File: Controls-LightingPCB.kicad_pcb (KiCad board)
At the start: 2 copper layers, 80.3 x 98.8 mm, 92 parts, among them J1 MinionConn, J10 INTERNAL_RIGHTBLINK, J11 INTERNAL_LEFTBLINK, J12 EXTERNAL_RIGHTBLINK, J13 EXTERNAL_HDLT, J14 EXTERNAL_BRAKELIGHT, J2 12VPWRCONN, J3 CRUZ_ST_INDICATOR_33v, J4 CRUZ_EN_INDICATOR_33v, J5 REGEN_INDICATOR_33v, J6 NEU_INDICATOR_33v, J7 FOR_INDICATOR_33v, J8 REV_INDICATOR_33v, J9 EXTERNAL_LEFTBLINK, Q1 2N7000, Q2 2N7000, Q3 2N7000, Q4 2N7000, Q5 2N7000, SW1 CRUISE_SET, SW2 CRUISE_ENABLE, SW3 F/R_SW, SW4 REGEN_SW, SW5 TURN_SIGNAL_SW, U1 NCP1117-3.3_SOT223

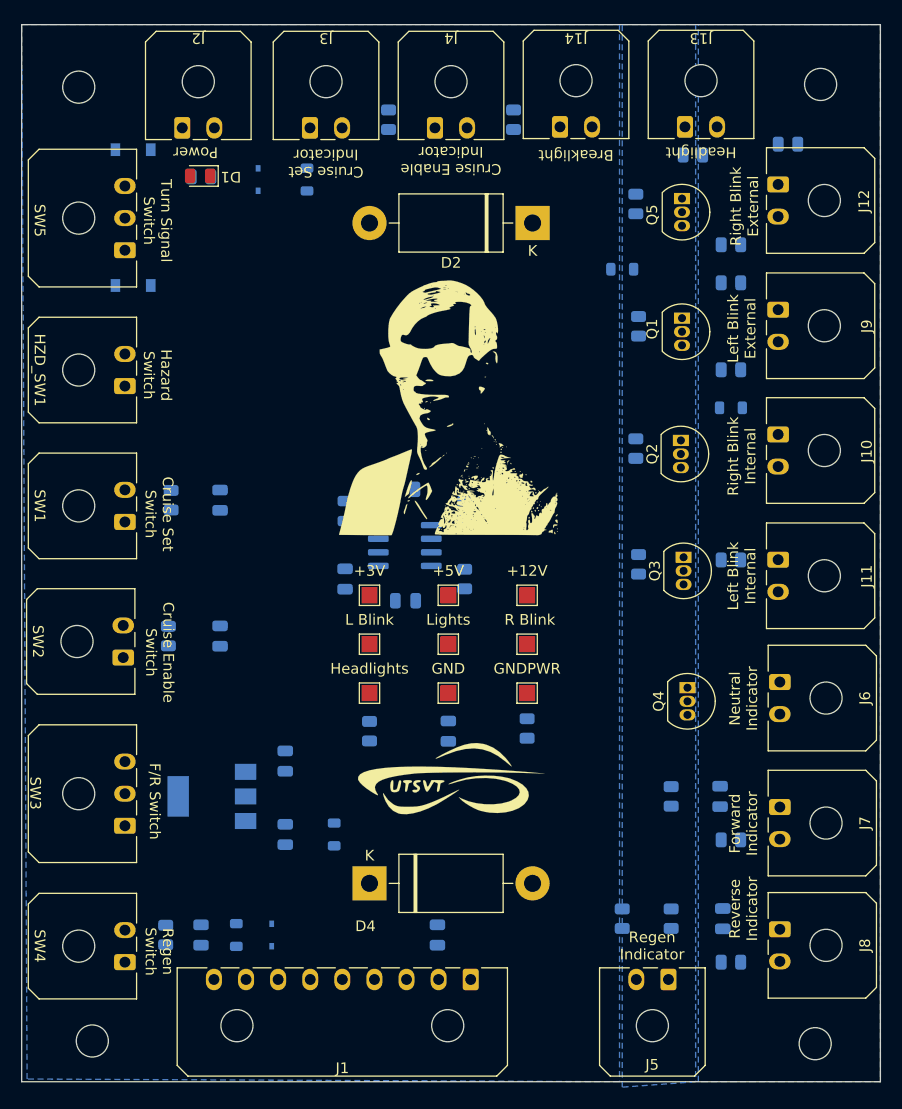
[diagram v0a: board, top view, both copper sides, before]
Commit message: Pico-Claps connectors + traces
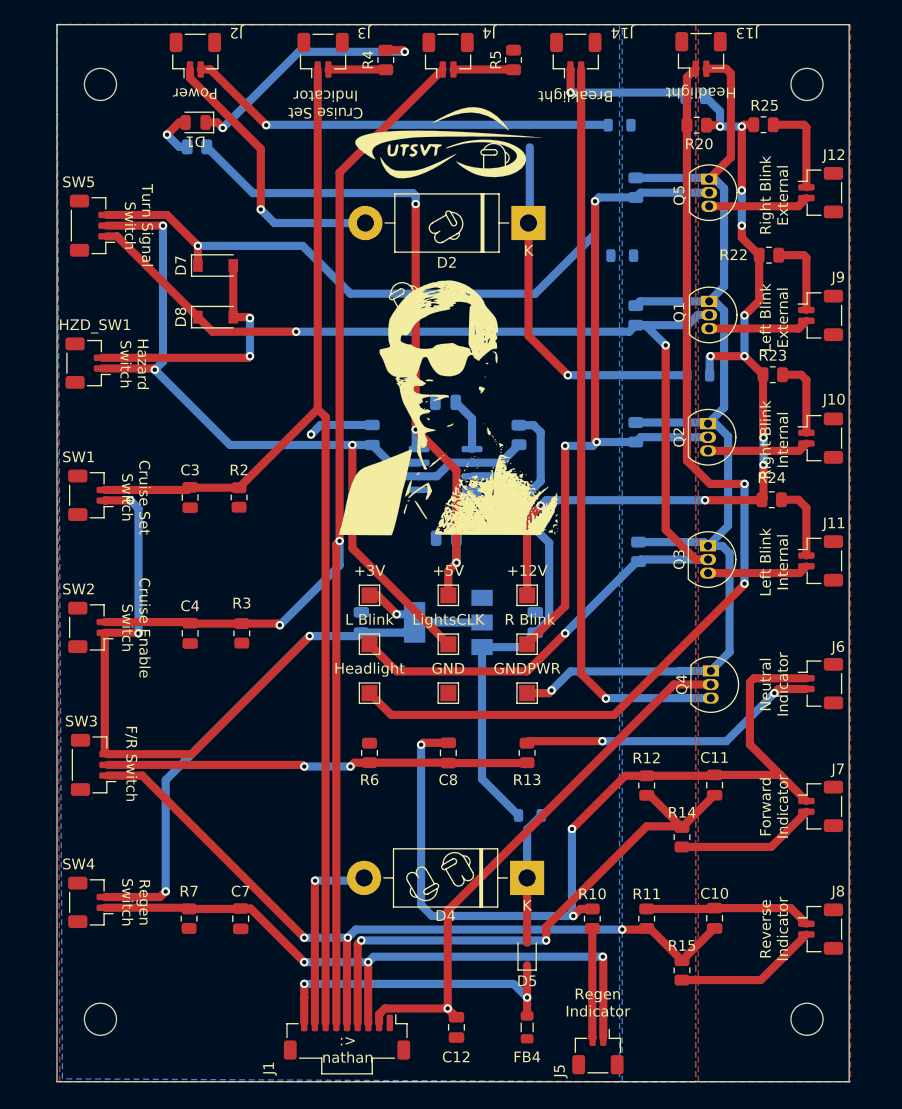
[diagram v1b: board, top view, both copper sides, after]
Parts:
- C10, C11, C12, C3, C4, C7, C8, D5, D7, D8, FB4, R10, R11, R12, R13, R14, R15, R2, R20, R22, R23, R24, R25, R3, R4, R5, R6, R7: moved to F.Cu
- HZD_SW1, J10, J11, J12, J13, J14, J2, J3, J4, J5, J6, J7, J8, J9, SW1, SW2, SW4: footprint Connector_Molex:Molex_Micro-Fit_3.0_43650-0200_1x02_P3.00mm_Horizontal -> Connector_Molex:Molex_Pico-Clasp_501331-0207_1x02-1MP_P1.00mm_Vertical
- J1: footprint Connector_Molex:Molex_Micro-Fit_3.0_43650-0900_1x09_P3.00mm_Horizontal -> Connector_Molex:Molex_Pico-Clasp_501331-0907_1x09-1MP_P1.00mm_Vertical
- SW3, SW5: footprint Connector_Molex:Molex_Micro-Fit_3.0_43650-0300_1x03_P3.00mm_Horizontal -> Connector_Molex:Molex_Pico-Clasp_501331-0307_1x03-1MP_P1.00mm_Vertical
- moved LOGO2 59.4 mm to (144.0, 55.1)
- moved C1 30.6 mm to (152.4, 99.8), turned to 90 degrees
- moved FB2 29.6 mm to (160.3, 53.3), turned to 0 degrees
- moved FB4 28.5 mm to (151.6, 137.7), turned to -90 degrees
- moved U1 27.4 mm to (144.3, 99.8)
- moved D3 25.7 mm to (151.9, 54.4)
- moved D5 23.9 mm to (151.6, 130.8)
- moved FB3 18.4 mm to (151.9, 117.9), turned to 180 degrees
- moved C2 14.8 mm to (136.1, 99.8)
- moved D4 14.7 mm to (151.6, 123.7), turned to 180 degrees
- moved R21 14.2 mm to (167.4, 50.7)
- moved D7 13.3 mm to (122.5, 66.5)
- moved J1 12.8 mm to (134.8, 138.6)
- moved J5 9.44 mm to (158.3, 140.0)
- moved C5 8.98 mm to (144.0, 79.2)
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- renumbered Headlights to Headlight, Lights to LightsCLK
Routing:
- net GND: track 0.00 -> 128.0 mm, vias 0 -> 6
- net /LEFT_BLINK: track 0.07 -> 123.6 mm, vias 0 -> 3
- net /RIGHT_BLINK: track 0.00 -> 123.2 mm, vias 0 -> 4
- net /CRUZ_EN: track 0.00 -> 119.9 mm, vias 0 -> 2
- net /CRUZ_ST: track 0.00 -> 112.5 mm
- net GNDPWR: track 0.26 -> 111.8 mm, vias 0 -> 1
- net +5V: track 0.00 -> 110.9 mm, vias 0 -> 3
- net +3V3: track 0.00 -> 110.5 mm, vias 0 -> 5
- net /HEADLIGHT_SW: track 0.03 -> 93.6 mm, vias 0 -> 2
- net +12V: track 0.00 -> 80.0 mm, vias 0 -> 11
- net /LIGHTSCLK: track 0.00 -> 74.7 mm, vias 0 -> 3
- net /REV_SW: track 0.00 -> 73.9 mm, vias 0 -> 3
- net Net-(J14-Pad2): track 0.00 -> 69.6 mm, vias 0 -> 1
- net /REGEN_SW: track 0.00 -> 62.2 mm, vias 0 -> 3
- net /FOR_SW: track 0.00 -> 51.9 mm, vias 0 -> 2
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- added copper zone on F.Cu, net +12V
- added copper zone on F.Cu, net GND
- removed copper zone on B.Cu, net +12V
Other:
- board size 80.3 x 98.8 mm -> 74 x 98.8 mm
- board text added: ":> nathan"
- board text removed: "Cruise Enable Indicator"

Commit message: Changes to traces/silkscreens
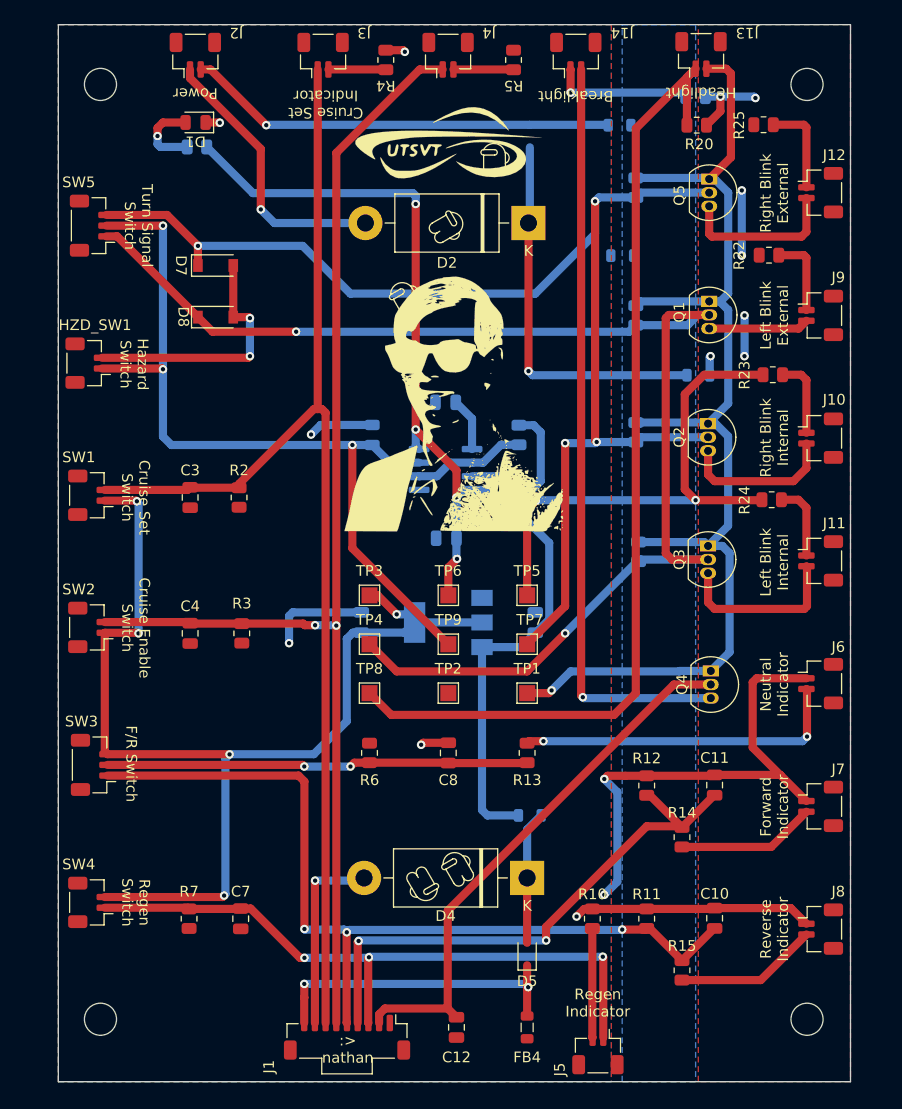
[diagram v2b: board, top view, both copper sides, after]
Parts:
- TP4: renamed from L Blink
- TP7: renamed from R Blink
- moved LOGO1 0.62 mm to (143.9, 79.1)
- renumbered GNDPWR to TP1, GND to TP2, +3V to TP3, +12V to TP5, +5V to TP6, Headlight to TP8, LightsCLK to TP9
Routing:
- net GND: track 128.0 -> 90.5 mm, vias 6 -> 8
- net +12V: track 80.0 -> 68.5 mm, vias 11 -> 9
- net /REV_SW: track 73.9 -> 82.0 mm
- net Net-(J11-Pad2): track 9.46 -> 16.1 mm
- net +3V3: track 110.5 -> 104.6 mm
- net Net-(J12-Pad2): track 9.41 -> 15.1 mm
- net Net-(J10-Pad2): track 9.48 -> 14.5 mm
- net /LEFT_BLINK: track 123.6 -> 128.1 mm, vias 3 -> 2
- net +5V: track 110.9 -> 107.0 mm, vias 3 -> 4
- net /CRUZ_EN: track 119.9 -> 116.3 mm
- net /LIGHTSCLK: track 74.7 -> 78.0 mm
- net Net-(J6-Pad2): track 28.2 -> 30.9 mm
- net Net-(D1-Pad2): track 4.56 -> 6.97 mm
- net Net-(D2-Pad1): track 34.0 -> 35.9 mm
- net /HEADLIGHT_SW: track 93.6 -> 92.4 mm, vias 2 -> 0
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
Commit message: edge cuts
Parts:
- moved H3 1.80 mm to (112.0, 138.7)
- moved H4 1.78 mm to (177.8, 138.7)
- moved H1 1.55 mm to (112.0, 48.0)
- moved H2 1.52 mm to (177.8, 48.0)
- moved SW3 0.35 mm to (110.7, 113.1)
- moved SW5 0.25 mm to (110.7, 62.7)
- moved HZD_SW1 0.16 mm to (110.7, 75.6)
- moved SW1 0.09 mm to (110.7, 87.9)
- moved SW2 0.09 mm to (110.7, 100.3)
- moved SW4 0.09 mm to (110.7, 126.0)
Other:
- board size 74 x 98.8 mm -> 73.9 x 98.8 mm
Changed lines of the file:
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@@
   (net 44 "Net-(D7-Pad2)")
   (footprint "Connector_Molex:Molex_Pico-Clasp_501331-0307_1x03-1MP_P1.00mm_Vertical" (layer "F.Cu")
-    (at 111.092 113.132855 90)
+    (at 110.744 113.132855 90)
     (descr "Molex Pico-Clasp series connector, 501331-0307 (http://www.molex.com/pdm_docs/sd/5013310207_sd.pdf), generated with kicad-footprint-generator")
     (tags "connector Molex Pico-Clasp side entry")
@@
   )
   (footprint "MountingHole:MountingHole_3mm" (layer "F.Cu")
-    (at 111.76 49.53)
+    (at 112.014 48.006)
     (descr "Mounting Hole 3mm, no annular")
     (tags "mounting hole 3mm no annular")
@@
       (net 41 "/HEADLIGHT_SW") (pinfunction "1") (pintype "passive"))
   )
-  (footprint "MountingHole:MountingHole_3mm" locked (layer "F.Cu")
-    (at 177.8 49.53)
+  (footprint "MountingHole:MountingHole_3mm" (layer "F.Cu")
+    (at 177.8 48.006)
     (descr "Mounting Hole 3mm, no annular")
     (tags "mounting hole 3mm no annular")
@@
   )
   (footprint "Connector_Molex:Molex_Pico-Clasp_501331-0207_1x02-1MP_P1.00mm_Vertical" (layer "F.Cu")
-    (at 110.584 75.581142 90)
+    (at 110.744 75.581142 90)
     (descr "Molex Pico-Clasp series connector, 501331-0207 (http://www.molex.com/pdm_docs/sd/5013310207_sd.pdf), generated with kicad-footprint-generator")
     (tags "connector Molex Pico-Clasp side entry")
@@
   )
   (footprint "Connector_Molex:Molex_Pico-Clasp_501331-0307_1x03-1MP_P1.00mm_Vertical" (layer "F.Cu")
-    (at 110.998 62.730571 90)
+    (at 110.744 62.730571 90)
     (descr "Molex Pico-Clasp series connector, 501331-0307 (http://www.molex.com/pdm_docs/sd/5013310207_sd.pdf), generated with kicad-footprint-generator")
     (tags "connector Molex Pico-Clasp side entry")
@@
   )
   (footprint "MountingHole:MountingHole_3mm" (layer "F.Cu")
-    (at 111.76 136.906)
+    (at 112.014 138.684)
     (descr "Mounting Hole 3mm, no annular")
     (tags "mounting hole 3mm no annular")
@@
   )
   (footprint "Connector_Molex:Molex_Pico-Clasp_501331-0207_1x02-1MP_P1.00mm_Vertical" (layer "F.Cu")
-    (at 110.838 125.983426 90)
+    (at 110.744 125.983426 90)
     (descr "Molex Pico-Clasp series connector, 501331-0207 (http://www.molex.com/pdm_docs/sd/5013310207_sd.pdf), generated with kicad-footprint-generator")
     (tags "connector Molex Pico-Clasp side entry")
@@
   )
   (footprint "Connector_Molex:Molex_Pico-Clasp_501331-0207_1x02-1MP_P1.00mm_Vertical" (layer "F.Cu")
-    (at 110.838 100.282284 90)
+    (at 110.744 100.282284 90)
     (descr "Molex Pico-Clasp series connector, 501331-0207 (http://www.molex.com/pdm_docs/sd/5013310207_sd.pdf), generated with kicad-footprint-generator")
     (tags "connector Molex Pico-Clasp side entry")
@@
     )
   )
-  (footprint "MountingHole:MountingHole_3mm" locked (layer "F.Cu")
-    (at 177.8 136.906)
+  (footprint "MountingHole:MountingHole_3mm" (layer "F.Cu")
+    (at 177.8 138.684)
     (descr "Mounting Hole 3mm, no annular")
     (tags "mounting hole 3mm no annular")
@@
   )
   (footprint "Connector_Molex:Molex_Pico-Clasp_501331-0207_1x02-1MP_P1.00mm_Vertical" (layer "F.Cu")
-    (at 110.838 87.931713 90)
+    (at 110.744 87.931713 90)
     (descr "Molex Pico-Clasp series connector, 501331-0207 (http://www.molex.com/pdm_docs/sd/5013310207_sd.pdf), generated with kicad-footprint-generator")
     (tags "connector Molex Pico-Clasp side entry")
@@
   (gr_arc (start 144.036236 122.886177) (mid 143.689266 122.793207) (end 143.782236 122.446236) (layer "F.SilkS") (width 0.12))
   (gr_arc (start 143.782236 122.446236) (mid 144.564232 121.372056) (end 145.796 121.870177) (layer "F.SilkS") (width 0.12))
-  (gr_rect (start 181.864 43.942) (end 107.823 142.748) (layer "Edge.Cuts") (width 0.05) (fill none))
+  (gr_line (start 181.864 48.006) (end 181.864 138.684) (layer "Edge.Cuts") (width 0.05))
+  (gr_line (start 107.95 138.684) (end 107.95 48.006) (layer "Edge.Cuts") (width 0.05))
+  (gr_line (start 177.8 142.748) (end 112.014 142.748) (layer "Edge.Cuts") (width 0.05))
+  (gr_arc (start 177.8 43.942) (mid 180.673682 45.132318) (end 181.864 48.006) (layer "Edge.Cuts") (width 0.05))
+  (gr_line (start 112.014 43.942) (end 177.8 43.942) (layer "Edge.Cuts") (width 0.05))
+  (gr_arc (start 181.864 138.684) (mid 180.673682 141.557682) (end 177.8 142.748) (layer "Edge.Cuts") (width 0.05))
+  (gr_arc (start 107.95 48.006) (mid 109.140318 45.132318) (end 112.014 43.942) (layer "Edge.Cuts") (width 0.05))
+  (gr_arc (start 112.014 142.748) (mid 109.140318 141.557682) (end 107.95 138.684) (layer "Edge.Cuts") (width 0.05))
   (gr_text ":>\nnathan" (at 134.874 139.7) (layer "F.SilkS")
     (effects (font (size 1 1) (thickness 0.15)))
@@
     (effects (font (size 1 1) (thickness 0.25)))
   )
-  (gr_text "Turn Signal\nSwitch" (at 115.316 62.738 270) (layer "F.SilkS")
+  (gr_text "Turn Signal\nSwitch" (at 115.062 62.738 270) (layer "F.SilkS")
     (effects (font (size 1 1) (thickness 0.25)))
   )
@@
     (effects (font (size 1 1) (thickness 0.25)))
   )
-  (gr_text "Hazard\nSwitch" (at 114.902 75.692 270) (layer "F.SilkS")
+  (gr_text "Hazard\nSwitch" (at 115.062 75.692 270) (layer "F.SilkS")
     (effects (font (size 1 1) (thickness 0.25)))
   )

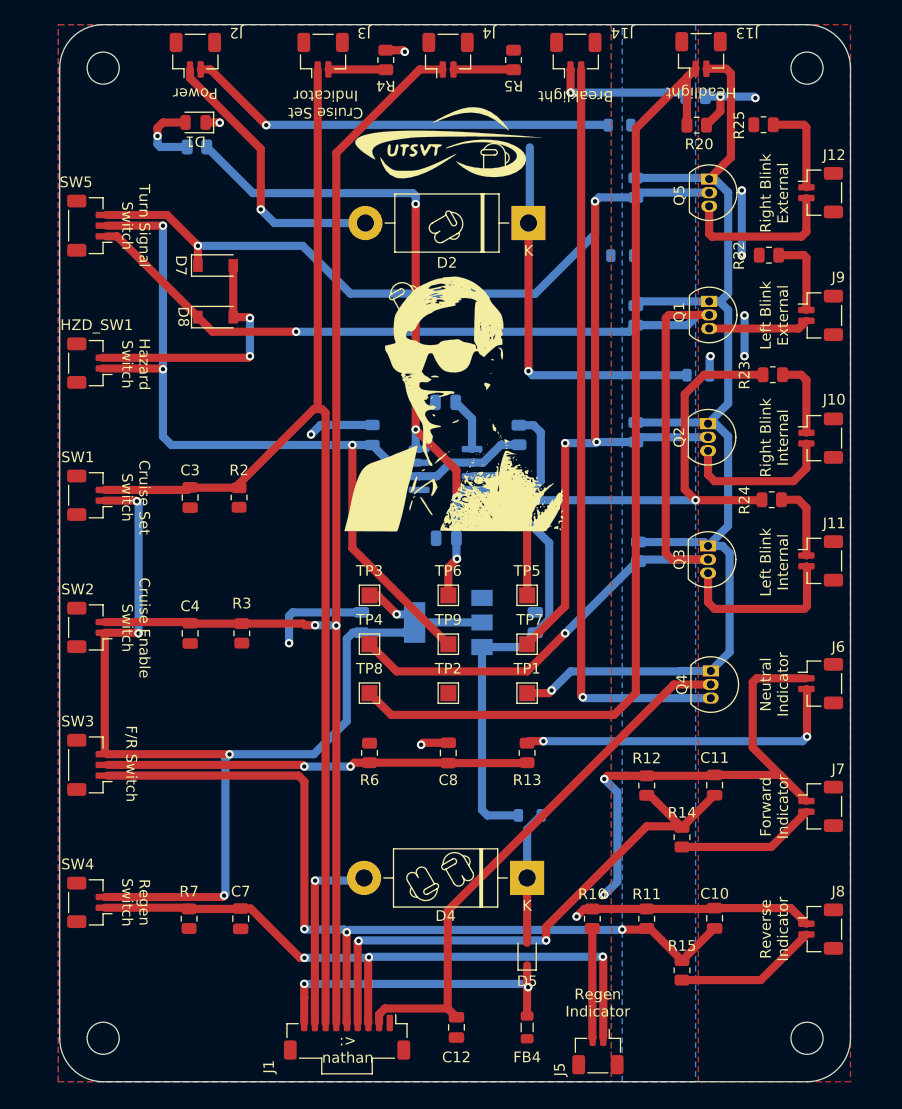
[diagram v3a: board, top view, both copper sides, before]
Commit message: moved components to front, fixed traces/planes
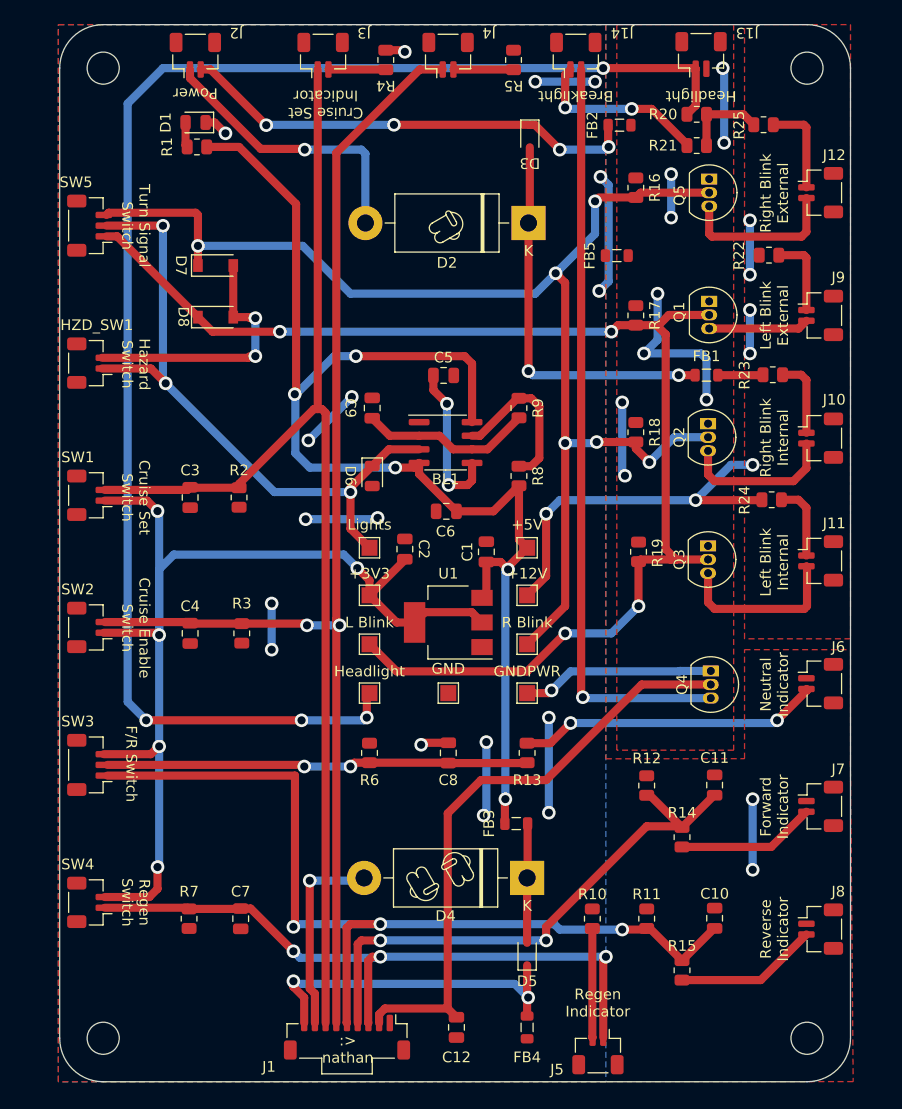
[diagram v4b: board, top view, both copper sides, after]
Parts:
- BL1, C1, C2, C5, C6, C9, D3, D6, FB1, FB2, FB3, FB5, R1, R16, R17, R18, R19, R21, R8, R9, U1: moved to F.Cu
- L Blink: renamed from TP4
- LOGO1, LOGO2: moved to B.Cu
- R Blink: renamed from TP7
- moved LOGO2 40.8 mm to (145.0, 95.9), turned to 180 degrees
- moved Lights 11.6 mm to (136.9, 92.8)
- moved C9 8.87 mm to (137.2, 79.8), turned to 90 degrees
- moved +5V 8.60 mm to (151.6, 92.8)
- moved C1 8.03 mm to (147.8, 93.2)
- moved C2 7.97 mm to (140.2, 93.0)
- moved R21 4.57 mm to (167.5, 55.2)
- moved D6 3.83 mm to (137.2, 86.1), turned to -90 degrees
- moved C5 2.52 mm to (143.8, 76.7), turned to 0 degrees
- moved R8 2.52 mm to (150.9, 86.1)
- moved R9 2.52 mm to (150.9, 79.8)
- moved BL1 2.52 mm to (144.0, 83.0)
- moved C6 2.52 mm to (144.1, 89.4)
- moved LOGO1 1.66 mm to (145.6, 79.1), turned to 180 degrees
- moved FB3 1.48 mm to (150.6, 118.6)
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- renumbered TP5 to +12V, TP3 to +3V3, TP6 to +5V, TP2 to GND, TP1 to GNDPWR, TP8 to Headlight, TP9 to Lights
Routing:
- net GNDPWR: track 112.3 -> 52.1 mm, vias 1 -> 10
- net /HEADLIGHT_SW: track 92.4 -> 140.6 mm, vias 0 -> 4
- net GND: track 90.5 -> 63.2 mm, vias 8 -> 19
- net /LIGHTSCLK: track 78.0 -> 62.4 mm
- net +5V: track 107.0 -> 121.4 mm, vias 4 -> 5
- net +12V: track 68.5 -> 56.8 mm, vias 9 -> 7
- net Net-(BL1-Pad5): track 5.00 -> 14.8 mm, vias 0 -> 2
- net /LEFT_BLINK: track 128.1 -> 122.7 mm, vias 2 -> 4
- net /BRAKELIGHT: track 51.1 -> 56.4 mm
- net Net-(D1-Pad2): track 6.97 -> 2.35 mm, vias 1 -> 0
- net /REV_SW: track 82.0 -> 86.1 mm
- net Net-(J14-Pad1): track 13.1 -> 16.6 mm, vias 1 -> 2
- net Net-(D3-Pad1): track 40.3 -> 43.4 mm, vias 1 -> 4
- net /RIGHT_BLINK: track 123.3 -> 120.3 mm, vias 4 -> 6
- net Net-(J6-Pad2): track 30.9 -> 28.4 mm
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- added copper zone on F.Cu, net GNDPWR
- removed copper zone on B.Cu, net GNDPWR
